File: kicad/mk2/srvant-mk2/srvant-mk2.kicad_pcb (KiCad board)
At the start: 4 copper layers, 104.8 x 148.1 mm, 254 parts, among them J10 HDMI connector, J11 USB A, J12 Screw_Terminal_01x02, J2 Conn_01x02, J3 Conn_01x03, J4 USB_OTG, J5 ARJM11, J8 Bus_M.2_Socket_M, J9 ARJM11, Q1 DMP3013SFV-7, SW1 POWER, SW2 EMMC_KEY, SW3 RST, SW4 HOST_RESET, U1 AP63205WU, U10 TPD4EUSB30, U11 TPD4EUSB30, U12 KSZ9131RNXI-TR, U13 74AHC1G04, U14 AP22653W6, U15 TLV62585DRLR, U16 FSUSB42MUX, U17 PCF85063AT/AAZ, U18 74LVC1G07SE-7, U19 TPD4EUSB30, U2 AP64501SP-13, U20 TPD4EUSB30, U21 74LVC1G07SE-7, U22 TMP1075DSG, U23 SLB9670VQ20FW785XTMA1, U24 74AHC1G08, U25 74AHC1G08, U3 74AHC1G32, U4 INA219AxDCN, U5 rp-t113-s3, U6 PCF85063AT/AAZ, U7 TPD4EUSB30, U8 74LVC2G07, U9 RT9742SNGV, Y1 X32K768S301, Y2 25Mhz, Y3 X32K768S301

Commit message: small changes to routing
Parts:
- moved TP11 2.79 mm to (19.0, 160.9)
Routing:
- net /bmc/BMC_HOST_POST_COMPLETE: track 95.2 -> 86.4 mm
- net /cm4/+3.3v_HOST: track 285.4 -> 291.9 mm
- net GND: track 310.2 -> 305.3 mm, vias 401 -> 426
- net /bmc/BMC_HOST_BT_nDis: track 58.4 -> 54.8 mm
- net /bmc/BMC_HOST_POWER_OUT: track 102.2 -> 98.6 mm
- net Net-(D8-K): track 7.41 -> 4.20 mm
- net /cm4/+5v_HOST: track 456.1 -> 458.9 mm
- net /cm4/GLOBAL_EN: track 47.8 -> 49.0 mm
- net /cm4/nPWR_LED: track 48.5 -> 49.3 mm
- net /cm4/+5v_HOST_VBUS: track 36.1 -> 36.7 mm, vias 2 -> 0
- net Net-(Module1A-PI_nLED_Activity): track 69.7 -> 69.1 mm
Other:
- board text added: "Project: SRVANT Board: Shepard Pi Revision: ${REVISION}"

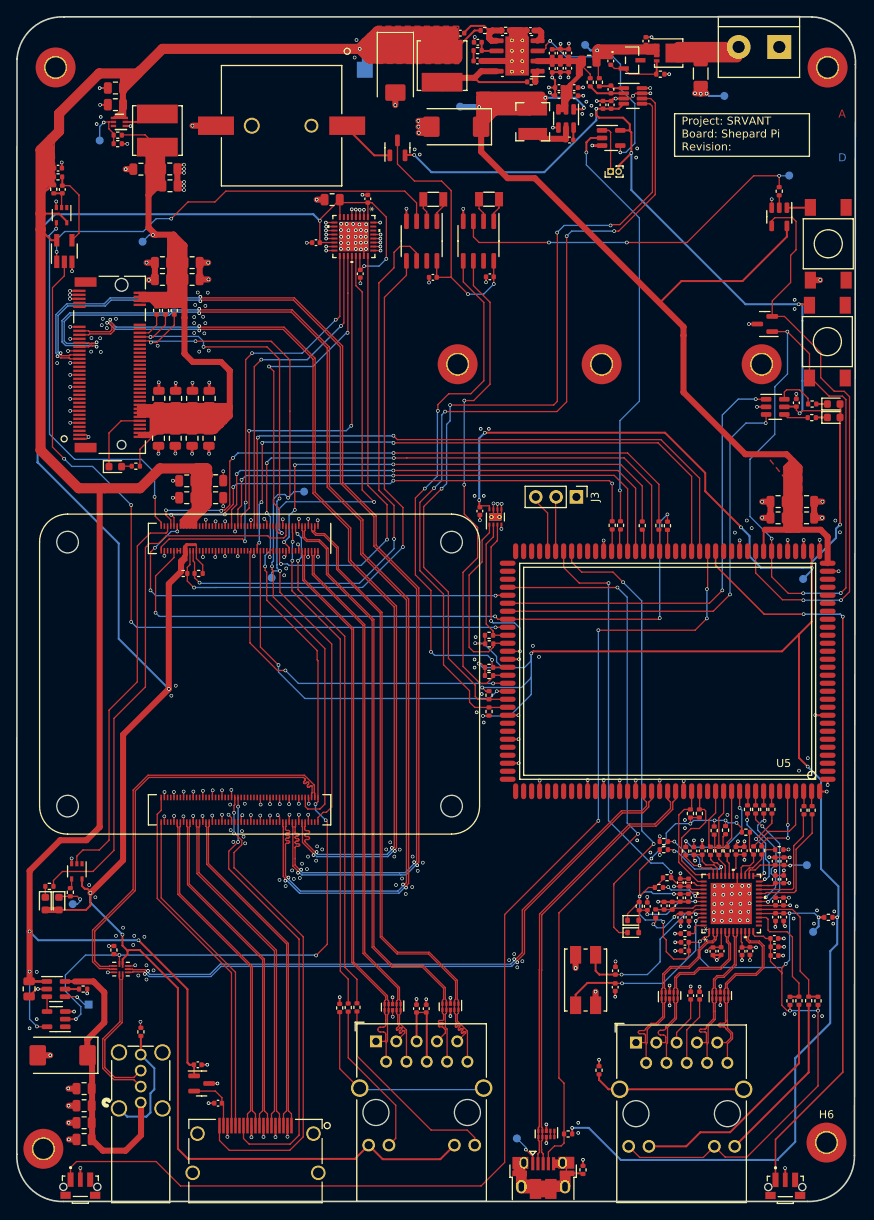
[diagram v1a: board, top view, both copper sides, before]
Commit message: lot's of small updates
* fix the quartz footprint
* fix wrong inductor in pcie power unit
* fix lots of descriptions,uids
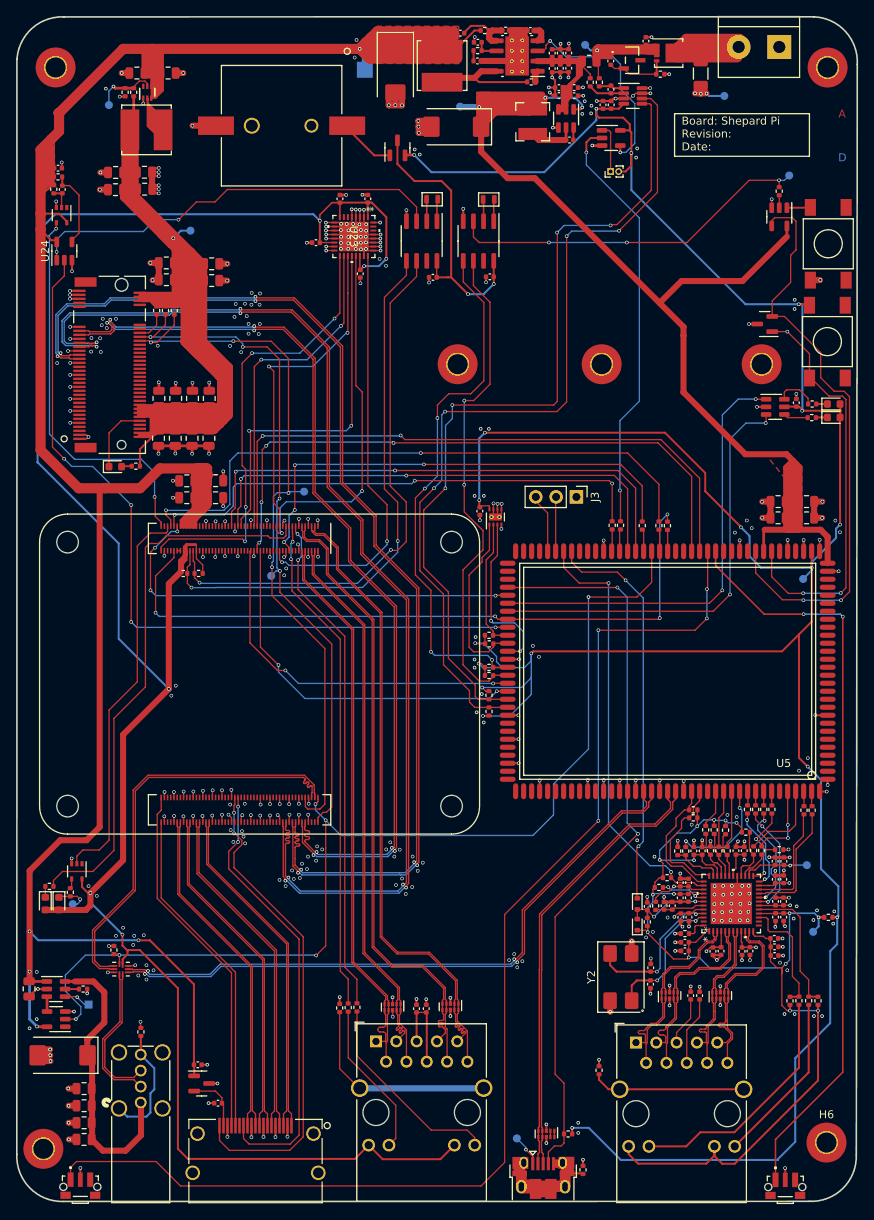
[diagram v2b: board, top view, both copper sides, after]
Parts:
- added C100: 10u, Capacitor_SMD:C_0805_2012Metric, F.Cu at (24.3, 71.6)
- C16, C20: value 220pF -> 220p
- C17: value 1.2nF -> 1200p
- C24, C28: value 100uF -> 100u
- C94: footprint Capacitor_SMD:C_0805_2012Metric -> Capacitor_SMD:C_0402_1005Metric
- L3: value 3.3µH -> 1µH
- U24: footprint Package_TO_SOT_SMD:SOT-23-5_HandSoldering -> Package_TO_SOT_SMD:SOT-23-5
- Y1, Y3: footprint Crystal:Crystal_SMD_3215-2Pin_3.2x1.5mm -> PCM_Crystal_AKL:Crystal_SMD_2012-2Pin_2.0x1.2mm
- Y2: footprint footprints:LFXTAL-25MHz -> PCM_Crystal_AKL:Crystal_SMD_FOX_FQ7050-4Pin_7.0x5.0mm
- moved C71 6.84 mm to (30.9, 57.0), turned to 0 degrees
- moved R55 6.50 mm to (25.5, 59.4), turned to -90 degrees
- moved TP12 6.15 mm to (33.7, 76.7)
- moved R28 5.84 mm to (98.7, 154.2), turned to 90 degrees
- moved R54 5.72 mm to (26.6, 59.4), turned to 90 degrees
- moved U15 5.09 mm to (28.3, 59.4), turned to 90 degrees
- moved C69 4.78 mm to (27.0, 57.0)
- moved TP6 4.58 mm to (23.5, 61.0)
- moved C68 4.43 mm to (91.2, 168.8)
- moved C67 4.43 mm to (91.2, 170.9)
- moved Y2 4.43 mm to (87.5, 170.0)
- moved D6 3.63 mm to (89.5, 160.8), turned to -90 degrees
- moved C78 3.19 mm to (27.9, 69.4)
- moved C80 3.19 mm to (28.0, 71.5)
- moved C76 3.19 mm to (24.3, 69.4)
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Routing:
- net /cm4/+3.3v_HOST_PCIe: track 241.2 -> 318.0 mm
- net Net-(U15-SW): track 7.10 -> 56.8 mm
- net GND: track 305.3 -> 348.4 mm, vias 426 -> 438
- net /cm4/USBOTG_ID: track 166.4 -> 135.1 mm, vias 9 -> 6
- net /bmc/EMMC_KEY: track 82.2 -> 51.7 mm, vias 4 -> 3
- net /cm4/+5v_HOST: track 458.9 -> 472.4 mm
- net /power/VIN: track 27.4 -> 36.6 mm
- net /BMC ethernet/3.3v_PHY: track 158.5 -> 150.6 mm
- net /BMC ethernet/RESET_OUT_N: track 57.8 -> 50.0 mm
- net Net-(U12-XI): track 23.5 -> 16.9 mm
- net Net-(J4-GND): track 39.7 -> 45.5 mm
- net /BMC ethernet/CLK125_EN: track 11.2 -> 6.28 mm, vias 2 -> 0
- net /BMC ethernet/PHYAD2: track 10.8 -> 6.24 mm, vias 2 -> 0
- net /cm4/HOST_SCL0: track 73.5 -> 69.7 mm
- net /cm4/HOST_SPI1_MOSI: track 48.5 -> 45.4 mm
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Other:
- board size 104.8 x 148.1 mm -> 105.1 x 148.1 mm
- board text added: "Board: Shepard Pi Revision: ${REVISION} Date: ${ISSUE_DATE}"
- board text removed: "Project: SRVANT Board: Shepard Pi Revision: ${REVISION}"

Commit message: fix drc
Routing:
- net /cm4/+3.3v_HOST_PCIe: track 318.0 -> 316.1 mm
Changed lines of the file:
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@@
     (property "rs#" "")
     (attr smd)
-    (fp_text reference "U23" (at 0 0 -90 unlocked) (layer "F.SilkS")
+    (fp_text reference "U23" (at 0 0 -90 unlocked) (layer "F.SilkS") hide
         (effects (font (size 1 1) (thickness 0.15)))
     )
-    (fp_text value "SLB9670VQ20FW785XTMA1" (at 0 0 -90 unlocked) (layer "F.Fab")
+    (fp_text value "SLB9670VQ20FW785XTMA1" (at 0 0 -90 unlocked) (layer "F.Fab") hide
         (effects (font (size 1 1) (thickness 0.15)))
     )
-    (fp_text user "*" (at -3.4417 -2 -90) (layer "F.SilkS")
+    (fp_text user "*" (at -3.4417 -2 90) (layer "F.SilkS") hide
         (effects (font (size 1 1) (thickness 0.15)))
     )
-    (fp_text user "*" (at -3.4417 -2 -90 unlocked) (layer "F.SilkS")
+    (fp_text user "*" (at -3.4417 -2 -90 unlocked) (layer "F.SilkS") hide
         (effects (font (size 1 1) (thickness 0.15)))
     )
-    (fp_text user "${REFERENCE}" (at 0 0 -90 unlocked) (layer "F.Fab")
+    (fp_text user "${REFERENCE}" (at 0 0 -90 unlocked) (layer "F.Fab") hide
         (effects (font (size 1 1) (thickness 0.15)))
     )
@@
         (effects (font (size 1 1) (thickness 0.15)))
     )
-    (fp_text user "*" (at -2.0447 -2 -90) (layer "F.Fab")
+    (fp_text user "*" (at -2.0447 -2 90) (layer "F.Fab")
         (effects (font (size 1 1) (thickness 0.15)))
     )
@@
   (via (at 23.495 166.114) (size 0.45) (drill 0.3) (layers "F.Cu" "B.Cu") (net 1))
   (via (at 21.28 91.82) (size 0.45) (drill 0.3) (layers "F.Cu" "B.Cu") (free) (net 1))
-  (via (at 40.51 85.83) (size 0.45) (drill 0.3) (layers "F.Cu" "B.Cu") (free) (net 1))
+  (via (at 40.52 85.88) (size 0.45) (drill 0.3) (layers "F.Cu" "B.Cu") (free) (net 1))
   (via (at 37.7952 111.1504) (size 0.45) (drill 0.3) (layers "F.Cu" "B.Cu") (net 1))
   (via (at 70.6424 83.1536) (size 0.45) (drill 0.3) (layers "F.Cu" "B.Cu") (net 1))
@@
   (via (at 83.9208 66.0556) (size 0.45) (drill 0.25) (layers "F.Cu" "B.Cu") (net 1))
   (via (at 103.632 167.9) (size 0.45) (drill 0.3) (layers "F.Cu" "B.Cu") (net 1))
-  (via (at 42.36 88.35) (size 0.45) (drill 0.3) (layers "F.Cu" "B.Cu") (free) (net 1))
+  (via (at 42.3 88.19) (size 0.45) (drill 0.3) (layers "F.Cu" "B.Cu") (free) (net 1))
   (via (at 99.19 159.68) (size 0.45) (drill 0.25) (layers "F.Cu" "B.Cu") (net 1))
   (via (at 58.48 61.02) (size 0.45) (drill 0.3) (layers "F.Cu" "B.Cu") (net 1))
-  (via (at 40.963 88.35) (size 0.45) (drill 0.3) (layers "F.Cu" "B.Cu") (free) (net 1))
+  (via (at 40.963 88.21) (size 0.45) (drill 0.3) (layers "F.Cu" "B.Cu") (free) (net 1))
   (via (at 107.8738 156.6672) (size 0.45) (drill 0.25) (layers "F.Cu" "B.Cu") (net 1))
   (via (at 105.16 110.582) (size 0.45) (drill 0.3) (layers "F.Cu" "B.Cu") (net 1))
@@
   (via (at 27.799998 60.8) (size 0.45) (drill 0.3) (layers "F.Cu" "B.Cu") (net 1))
   (via (at 101.2952 160.8074) (size 0.45) (drill 0.25) (layers "F.Cu" "B.Cu") (net 1))
-  (via (at 40.963 89.581) (size 0.45) (drill 0.3) (layers "F.Cu" "B.Cu") (free) (net 1))
+  (via (at 40.963 89.67) (size 0.45) (drill 0.3) (layers "F.Cu" "B.Cu") (free) (net 1))
   (via (at 102.37 162.9) (size 0.45) (drill 0.25) (layers "F.Cu" "B.Cu") (net 1))
   (via (at 69.469 136.906) (size 0.45) (drill 0.25) (layers "F.Cu" "B.Cu") (net 1))
@@
   (via (at 28.194 170.307) (size 0.45) (drill 0.3) (layers "F.Cu" "B.Cu") (free) (net 1))
   (via (at 89.408 67.564) (size 0.45) (drill 0.25) (layers "F.Cu" "B.Cu") (net 1))
-  (via (at 42.233 89.62) (size 0.45) (drill 0.3) (layers "F.Cu" "B.Cu") (free) (net 1))
+  (via (at 42.35 89.65) (size 0.45) (drill 0.3) (layers "F.Cu" "B.Cu") (free) (net 1))
   (via (at 82.169 189.484) (size 0.45) (drill 0.25) (layers "F.Cu" "B.Cu") (net 1))
   (via (at 103.5812 160.782) (size 0.45) (drill 0.25) (layers "F.Cu" "B.Cu") (net 1))
@@
   (segment (start 28.96 101.9722) (end 28.6822 102.25) (width 0.76) (layer "F.Cu") (net 50))
   (segment (start 32.33 85.135) (end 32.33 78.165) (width 0.76) (layer "F.Cu") (net 50))
-  (segment (start 29.885 77.175) (end 31.235 78.525) (width 0.76) (layer "F.Cu") (net 50))
   (segment (start 34.68 92.14) (end 35.16 92.14) (width 1.27) (layer "F.Cu") (net 50))
   (segment (start 29.75 98.62) (end 36.05 98.62) (width 0.13) (layer "F.Cu") (net 50))
@@
   (segment (start 100.17 193.34) (end 99.19 192.36) (width 0.25) (layer "F.Cu") (net 54))
   (segment (start 92.3184 157.5816) (end 91.7428 158.1572) (width 0.13) (layer "F.Cu") (net 54))
-  (segment (start 93.295 166.955) (end 93.1672 166.8272) (width 0.13) (layer "F.Cu") (net 54))
   (via (at 108.1024 168.3512) (size 0.45) (drill 0.3) (layers "F.Cu" "B.Cu") (net 54))
   (via (at 92.35 155.35) (size 0.45) (drill 0.25) (layers "F.Cu" "B.Cu") (net 54))

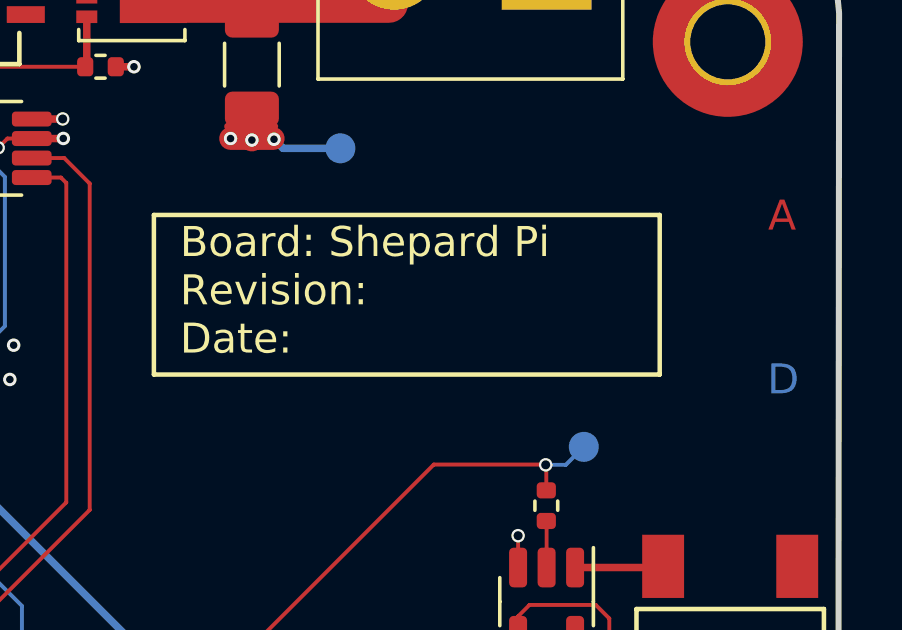
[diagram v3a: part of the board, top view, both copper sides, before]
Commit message: fix variable substitution
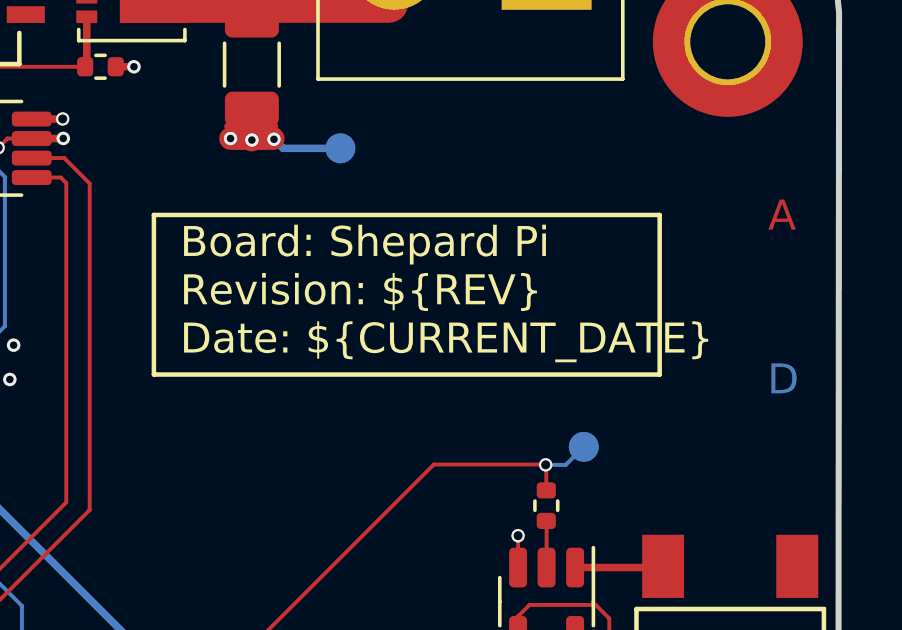
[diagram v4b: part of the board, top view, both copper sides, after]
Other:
- board text added: "Board: Shepard Pi Revision: ${REV} Date: ${CURRENT_DATE}"
- board text removed: "Board: Shepard Pi Revision: ${REVISION} Date: ${ISSUE_DATE}"
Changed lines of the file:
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@@
     (pad "2" smd roundrect (at 0.95 0 90) (size 1 1.45) (layers "F.Cu" "F.Paste" "F.Mask") (roundrect_rratio 0.25)
       (net 1 "GND") (pintype "passive"))
-    (model "${KICAD6_3DMODEL_DIR}/Capacitor_SMD.3dshapes/C_0805_2012Metric.wrl"
+    (model "${KICAD7_3DMODEL_DIR}/Capacitor_SMD.3dshapes/C_0805_2012Metric.wrl"
       (offset (xyz 0 0 0))
       (scale (xyz 1 1 1))
@@
     (pad "5" smd roundrect (at 1.1375 -0.95 90) (size 1.325 0.6) (layers "F.Cu" "F.Paste" "F.Mask") (roundrect_rratio 0.25)
       (net 344 "/cm4/+5v_HOST") (pinfunction "VCC") (pintype "power_in"))
-    (model "${KICAD6_3DMODEL_DIR}/Package_TO_SOT_SMD.3dshapes/SOT-23-5.wrl"
+    (model "${KICAD7_3DMODEL_DIR}/Package_TO_SOT_SMD.3dshapes/SOT-23-5.wrl"
       (offset (xyz 0 0 0))
       (scale (xyz 1 1 1))
@@
     (pad "2" smd roundrect (at 0.95 0 180) (size 1 1.45) (layers "F.Cu" "F.Paste" "F.Mask") (roundrect_rratio 0.25)
       (net 1 "GND") (pintype "passive"))
-    (model "${KICAD6_3DMODEL_DIR}/Capacitor_SMD.3dshapes/C_0805_2012Metric.wrl"
+    (model "${KICAD7_3DMODEL_DIR}/Capacitor_SMD.3dshapes/C_0805_2012Metric.wrl"
       (offset (xyz 0 0 0))
       (scale (xyz 1 1 1))
@@
     (pad "2" smd roundrect (at 0.95 0 180) (size 1 1.45) (layers "F.Cu" "F.Paste" "F.Mask") (roundrect_rratio 0.25)
       (net 1 "GND") (pintype "passive"))
-    (model "${KICAD6_3DMODEL_DIR}/Capacitor_SMD.3dshapes/C_0805_2012Metric.wrl"
+    (model "${KICAD7_3DMODEL_DIR}/Capacitor_SMD.3dshapes/C_0805_2012Metric.wrl"
       (offset (xyz 0 0 0))
       (scale (xyz 1 1 1))
@@
     (pad "2" smd roundrect (at 0.95 0 270) (size 1 1.45) (layers "F.Cu" "F.Paste" "F.Mask") (roundrect_rratio 0.25)
       (net 1 "GND") (pintype "passive"))
-    (model "${KICAD6_3DMODEL_DIR}/Capacitor_SMD.3dshapes/C_0805_2012Metric.wrl"
+    (model "${KICAD7_3DMODEL_DIR}/Capacitor_SMD.3dshapes/C_0805_2012Metric.wrl"
       (offset (xyz 0 0 0))
       (scale (xyz 1 1 1))
@@
     (pad "2" smd roundrect (at 0.48 0 90) (size 0.56 0.62) (layers "F.Cu" "F.Paste" "F.Mask") (roundrect_rratio 0.25)
       (net 1 "GND") (pintype "passive"))
-    (model "${KICAD6_3DMODEL_DIR}/Capacitor_SMD.3dshapes/C_0402_1005Metric.wrl"
+    (model "${KICAD7_3DMODEL_DIR}/Capacitor_SMD.3dshapes/C_0402_1005Metric.wrl"
       (offset (xyz 0 0 0))
       (scale (xyz 1 1 1))
@@
     (effects (font (size 1 1)) (justify left bottom))
   )
-  (gr_text "Board: Shepard Pi\nRevision: ${REVISION}\nDate: ${ISSUE_DATE}\n" (at 95.08 66.79) (layer "F.SilkS")
+  (gr_text "Board: Shepard Pi\nRevision: ${REV}\nDate: ${CURRENT_DATE}\n" (at 95.08 66.79) (layer "F.SilkS")
     (effects (font (size 1 1) (thickness 0.15)) (justify left bottom))
   )
